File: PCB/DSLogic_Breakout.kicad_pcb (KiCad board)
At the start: 2 copper layers, 5 parts, among them J1 Interconnect

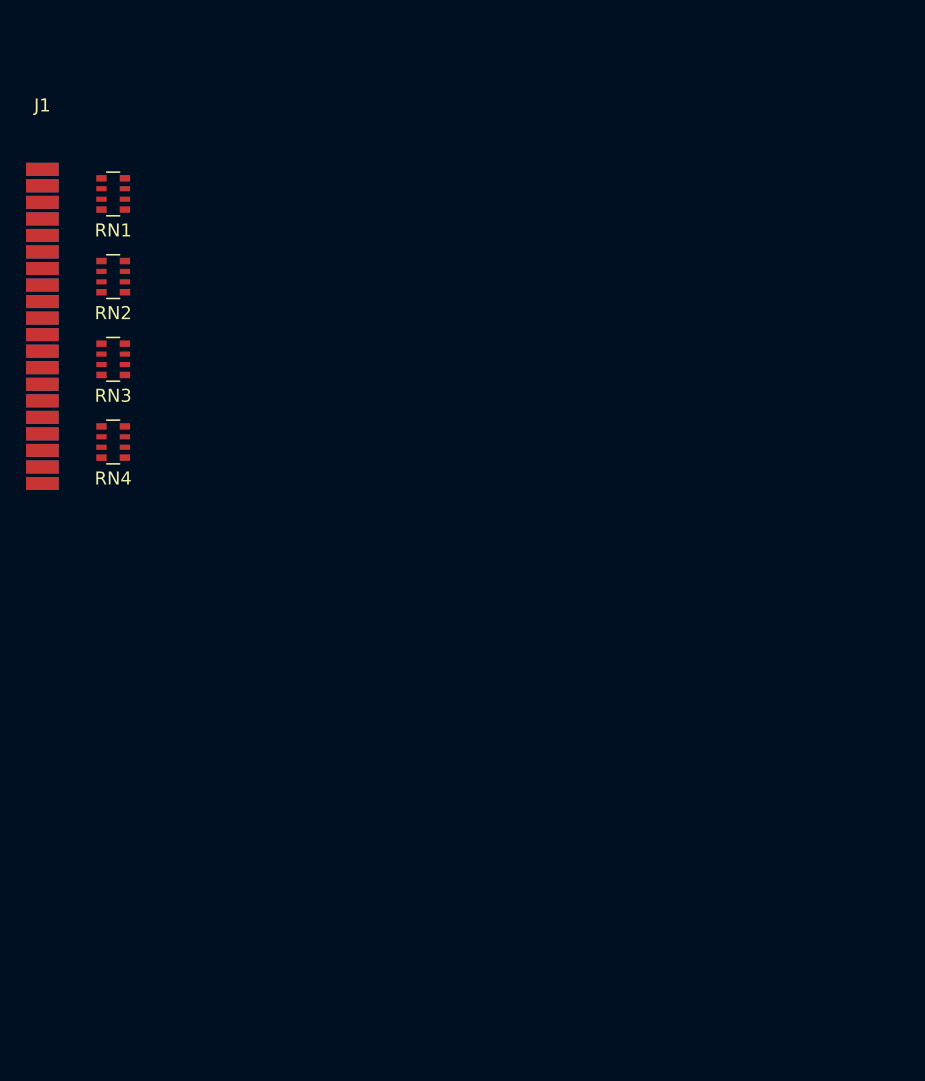
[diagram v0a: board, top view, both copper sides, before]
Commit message: Board max size measured
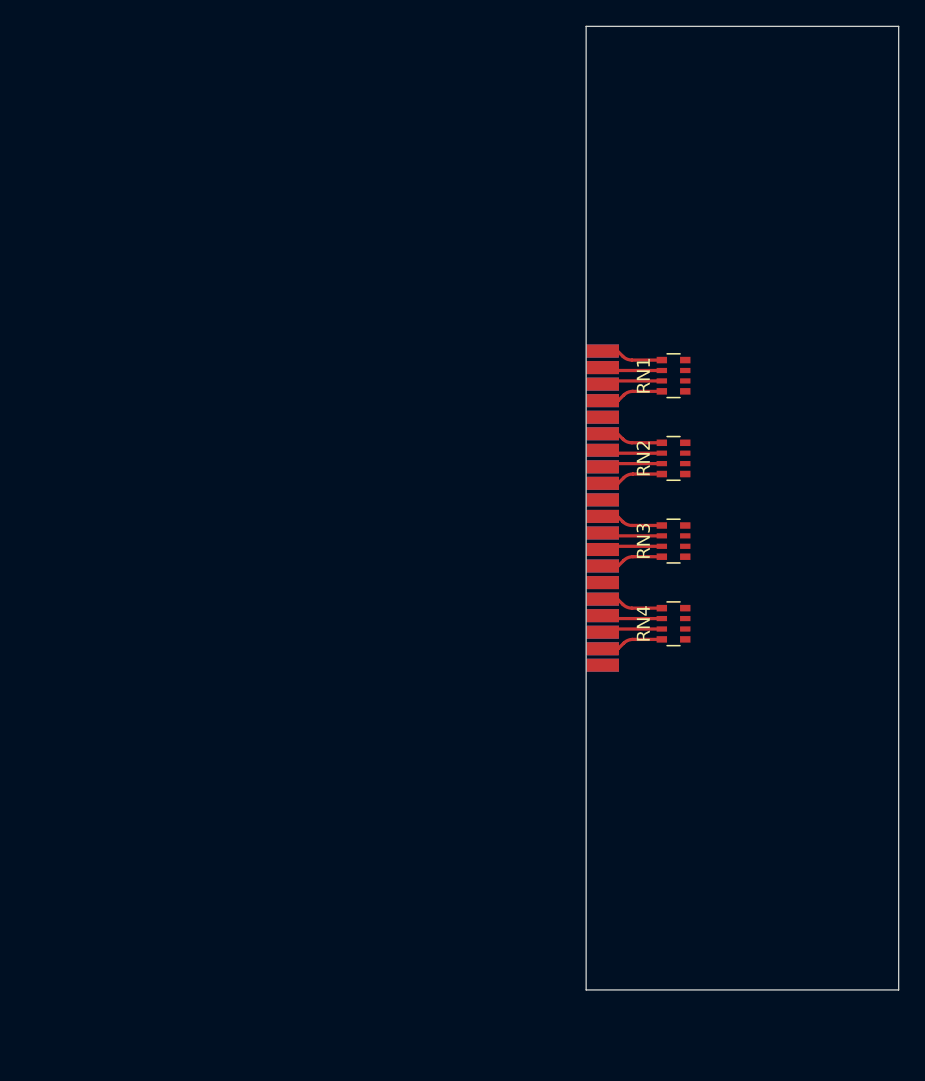
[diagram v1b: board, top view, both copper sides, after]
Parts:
- moved RN2 45.2 mm to (150.5, 59.9)
- moved RN3 45.2 mm to (150.5, 66.3)
- moved J1 45.2 mm to (145.0, 63.8)
- moved RN1 45.2 mm to (150.5, 53.6)
- moved RN4 45.2 mm to (150.5, 72.6)
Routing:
- net Net-(J1-Pin_7): track 0.00 -> 4.79 mm
- net Net-(J1-Pin_27): track 0.00 -> 4.79 mm
- net Net-(J1-Pin_17): track 0.00 -> 4.79 mm
- net Net-(J1-Pin_37): track 0.00 -> 4.79 mm
- net Net-(J1-Pin_11): track 0.00 -> 4.78 mm
- net Net-(J1-Pin_21): track 0.00 -> 4.78 mm
- net Net-(J1-Pin_1): track 0.00 -> 4.78 mm
- net Net-(J1-Pin_31): track 0.00 -> 4.78 mm
- net Net-(J1-Pin_5): track 0.00 -> 4.64 mm
- net Net-(J1-Pin_15): track 0.00 -> 4.64 mm
- net Net-(J1-Pin_35): track 0.00 -> 4.64 mm
- net Net-(J1-Pin_25): track 0.00 -> 4.64 mm
- net Net-(J1-Pin_33): track 0.00 -> 4.63 mm
- net Net-(J1-Pin_13): track 0.00 -> 4.63 mm
- net Net-(J1-Pin_3): track 0.00 -> 4.63 mm
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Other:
- board outline added: 24 x 74 mm
- board text added: "PCB Max Height: 74mm"

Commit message: Rev 1 Done
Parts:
- added ?: , , F.Cu at (141.1, 102.9)
- added ?: , , F.Cu at (123.3, 102.9)
- added ?: , , F.Cu at (125.9, 102.9)
- added ?: , , F.Cu at (133.5, 102.9)
- added ?: , , F.Cu at (141.1, 54.6)
- added ?: , , F.Cu at (133.5, 54.6)
- added ?: , , F.Cu at (151.3, 102.9)
- added ?: , , F.Cu at (146.2, 54.6)
- added ?: , , F.Cu at (156.3, 54.6)
- added ?: , , F.Cu at (138.6, 54.6)
- added ?: , , F.Cu at (136.0, 54.6)
- added ?: , , F.Cu at (151.3, 54.6)
- added ?: , , F.Cu at (123.3, 54.6)
- added ?: , , F.Cu at (146.2, 102.9)
- added ?: , , F.Cu at (148.7, 54.6)
- added ?: , , F.Cu at (153.8, 102.9)
- added ?: , , F.Cu at (130.9, 102.9)
- added ?: , , F.Cu at (130.9, 54.6)
- added ?: , , F.Cu at (120.8, 102.9)
- added ?: , , F.Cu at (128.4, 54.6)
- added ?: , , F.Cu at (156.3, 102.9)
- added ?: , , F.Cu at (128.4, 102.9)
- added ?: , , F.Cu at (148.7, 102.9)
- added ?: , , F.Cu at (143.6, 54.6)
- added ?: , , F.Cu at (153.8, 54.6)
- added ?: , , F.Cu at (138.6, 102.9)
- added ?: , , F.Cu at (143.6, 102.9)
- added ?: , , F.Cu at (136.0, 102.9)
- added ?: , , F.Cu at (125.9, 54.6)
- added D1: PWR, LED_SMD:LED_0603_1608Metric, F.Cu at (107.1, 56.1)
- added J2: Conn_Input, Connector_PinSocket_2.54mm:PinSocket_1x20_P2.54mm_Vertical, F.Cu at (117.6, 54.6)
- added R1: 2K2, Resistor_SMD:R_0603_1608Metric, F.Cu at (107.1, 54.6)
- added REF**: Protoboard_Hole, Footprints:Protoboard_Hole, F.Cu at (125.9, 72.4)
- added REF**: Protoboard_Hole, Footprints:Protoboard_Hole, F.Cu at (156.3, 59.7)
- added REF**: Protoboard_Hole, Footprints:Protoboard_Hole, F.Cu at (128.4, 67.3)
- added REF**: Protoboard_Hole, Footprints:Protoboard_Hole, F.Cu at (125.9, 97.8)
- added REF**: Protoboard_Hole, Footprints:Protoboard_Hole, F.Cu at (128.4, 74.9)
- added REF**: Protoboard_Hole, Footprints:Protoboard_Hole, F.Cu at (156.3, 67.3)
- added REF**: Protoboard_Hole, Footprints:Protoboard_Hole, F.Cu at (141.1, 85.1)
- added REF**: Protoboard_Hole, Footprints:Protoboard_Hole, F.Cu at (133.5, 72.4)
- added REF**: Protoboard_Hole, Footprints:Protoboard_Hole, F.Cu at (141.1, 57.1)
- added REF**: Protoboard_Hole, Footprints:Protoboard_Hole, F.Cu at (123.3, 62.2)
- added REF**: Protoboard_Hole, Footprints:Protoboard_Hole, F.Cu at (141.1, 59.7)
- added REF**: Protoboard_Hole, Footprints:Protoboard_Hole, F.Cu at (128.4, 95.2)
- added REF**: Protoboard_Hole, Footprints:Protoboard_Hole, F.Cu at (146.2, 85.1)
- added REF**: Protoboard_Hole, Footprints:Protoboard_Hole, F.Cu at (156.3, 82.5)
- added REF**: Protoboard_Hole, Footprints:Protoboard_Hole, F.Cu at (120.8, 82.5)
- added REF**: Protoboard_Hole, Footprints:Protoboard_Hole, F.Cu at (148.7, 90.2)
- added REF**: Protoboard_Hole, Footprints:Protoboard_Hole, F.Cu at (146.2, 77.5)
- added REF**: Protoboard_Hole, Footprints:Protoboard_Hole, F.Cu at (151.3, 87.6)
- added REF**: Protoboard_Hole, Footprints:Protoboard_Hole, F.Cu at (151.3, 59.7)
- added REF**: Protoboard_Hole, Footprints:Protoboard_Hole, F.Cu at (143.6, 90.2)
- added REF**: Protoboard_Hole, Footprints:Protoboard_Hole, F.Cu at (153.8, 95.2)
- added REF**: Protoboard_Hole, Footprints:Protoboard_Hole, F.Cu at (138.6, 85.1)
- added REF**: Protoboard_Hole, Footprints:Protoboard_Hole, F.Cu at (125.9, 95.2)
- added REF**: Protoboard_Hole, Footprints:Protoboard_Hole, F.Cu at (125.9, 80.0)
- added REF**: Protoboard_Hole, Footprints:Protoboard_Hole, F.Cu at (143.6, 69.8)
- added REF**: Protoboard_Hole, Footprints:Protoboard_Hole, F.Cu at (123.3, 64.8)
- added REF**: Protoboard_Hole, Footprints:Protoboard_Hole, F.Cu at (128.4, 92.7)
- added REF**: Protoboard_Hole, Footprints:Protoboard_Hole, F.Cu at (156.3, 100.3)
- added REF**: Protoboard_Hole, Footprints:Protoboard_Hole, F.Cu at (136.0, 87.6)
- added REF**: Protoboard_Hole, Footprints:Protoboard_Hole, F.Cu at (123.3, 87.6)
- added REF**: Protoboard_Hole, Footprints:Protoboard_Hole, F.Cu at (156.3, 57.1)
- added REF**: Protoboard_Hole, Footprints:Protoboard_Hole, F.Cu at (156.3, 72.4)
- added REF**: Protoboard_Hole, Footprints:Protoboard_Hole, F.Cu at (151.3, 57.1)
- added REF**: Protoboard_Hole, Footprints:Protoboard_Hole, F.Cu at (133.5, 77.5)
- added REF**: Protoboard_Hole, Footprints:Protoboard_Hole, F.Cu at (153.8, 77.5)
- added REF**: Protoboard_Hole, Footprints:Protoboard_Hole, F.Cu at (120.8, 85.1)
- added REF**: Protoboard_Hole, Footprints:Protoboard_Hole, F.Cu at (123.3, 69.8)
- added REF**: Protoboard_Hole, Footprints:Protoboard_Hole, F.Cu at (146.2, 62.2)
- added REF**: Protoboard_Hole, Footprints:Protoboard_Hole, F.Cu at (128.4, 100.3)
- added REF**: Protoboard_Hole, Footprints:Protoboard_Hole, F.Cu at (151.3, 80.0)
- added REF**: Protoboard_Hole, Footprints:Protoboard_Hole, F.Cu at (130.9, 97.8)
- added REF**: Protoboard_Hole, Footprints:Protoboard_Hole, F.Cu at (130.9, 59.7)
- added REF**: Protoboard_Hole, Footprints:Protoboard_Hole, F.Cu at (130.9, 72.4)
- added REF**: Protoboard_Hole, Footprints:Protoboard_Hole, F.Cu at (141.1, 87.6)
- added REF**: Protoboard_Hole, Footprints:Protoboard_Hole, F.Cu at (120.8, 87.6)
- added REF**: Protoboard_Hole, Footprints:Protoboard_Hole, F.Cu at (141.1, 69.8)
- added REF**: Protoboard_Hole, Footprints:Protoboard_Hole, F.Cu at (148.7, 97.8)
- added REF**: Protoboard_Hole, Footprints:Protoboard_Hole, F.Cu at (130.9, 62.2)
- added REF**: Protoboard_Hole, Footprints:Protoboard_Hole, F.Cu at (141.1, 62.2)
- added REF**: Protoboard_Hole, Footprints:Protoboard_Hole, F.Cu at (133.5, 59.7)
- added REF**: Protoboard_Hole, Footprints:Protoboard_Hole, F.Cu at (138.6, 69.8)
- added REF**: Protoboard_Hole, Footprints:Protoboard_Hole, F.Cu at (130.9, 92.7)
- added REF**: Protoboard_Hole, Footprints:Protoboard_Hole, F.Cu at (148.7, 77.5)
- added REF**: Protoboard_Hole, Footprints:Protoboard_Hole, F.Cu at (125.9, 69.8)
- added REF**: Protoboard_Hole, Footprints:Protoboard_Hole, F.Cu at (120.8, 67.3)
- added REF**: Protoboard_Hole, Footprints:Protoboard_Hole, F.Cu at (120.8, 72.4)
- added REF**: Protoboard_Hole, Footprints:Protoboard_Hole, F.Cu at (156.3, 92.7)
- added REF**: Protoboard_Hole, Footprints:Protoboard_Hole, F.Cu at (148.7, 82.5)
- added REF**: Protoboard_Hole, Footprints:Protoboard_Hole, F.Cu at (133.5, 100.3)
- added REF**: Protoboard_Hole, Footprints:Protoboard_Hole, F.Cu at (120.8, 62.2)
- added REF**: Protoboard_Hole, Footprints:Protoboard_Hole, F.Cu at (148.7, 57.1)
- added REF**: Protoboard_Hole, Footprints:Protoboard_Hole, F.Cu at (153.8, 82.5)
- added REF**: Protoboard_Hole, Footprints:Protoboard_Hole, F.Cu at (153.8, 87.6)
- added REF**: Protoboard_Hole, Footprints:Protoboard_Hole, F.Cu at (125.9, 62.2)
- added REF**: Protoboard_Hole, Footprints:Protoboard_Hole, F.Cu at (120.8, 95.2)
- added REF**: Protoboard_Hole, Footprints:Protoboard_Hole, F.Cu at (136.0, 64.8)
- added REF**: Protoboard_Hole, Footprints:Protoboard_Hole, F.Cu at (130.9, 100.3)
- added REF**: Protoboard_Hole, Footprints:Protoboard_Hole, F.Cu at (130.9, 69.8)
- added REF**: Protoboard_Hole, Footprints:Protoboard_Hole, F.Cu at (123.3, 59.7)
- added REF**: Protoboard_Hole, Footprints:Protoboard_Hole, F.Cu at (128.4, 87.6)
- added REF**: Protoboard_Hole, Footprints:Protoboard_Hole, F.Cu at (148.7, 85.1)
- added REF**: Protoboard_Hole, Footprints:Protoboard_Hole, F.Cu at (143.6, 87.6)
- added REF**: Protoboard_Hole, Footprints:Protoboard_Hole, F.Cu at (148.7, 92.7)
- added REF**: Protoboard_Hole, Footprints:Protoboard_Hole, F.Cu at (123.3, 57.1)
- added REF**: Protoboard_Hole, Footprints:Protoboard_Hole, F.Cu at (153.8, 72.4)
- added REF**: Protoboard_Hole, Footprints:Protoboard_Hole, F.Cu at (130.9, 80.0)
- added REF**: Protoboard_Hole, Footprints:Protoboard_Hole, F.Cu at (123.3, 77.5)
- added REF**: Protoboard_Hole, Footprints:Protoboard_Hole, F.Cu at (141.1, 77.5)
- added REF**: Protoboard_Hole, Footprints:Protoboard_Hole, F.Cu at (146.2, 82.5)
- added REF**: Protoboard_Hole, Footprints:Protoboard_Hole, F.Cu at (153.8, 80.0)
- added REF**: Protoboard_Hole, Footprints:Protoboard_Hole, F.Cu at (146.2, 87.6)
- added REF**: Protoboard_Hole, Footprints:Protoboard_Hole, F.Cu at (153.8, 69.8)
- added REF**: Protoboard_Hole, Footprints:Protoboard_Hole, F.Cu at (136.0, 57.1)
- added REF**: Protoboard_Hole, Footprints:Protoboard_Hole, F.Cu at (143.6, 72.4)
- added REF**: Protoboard_Hole, Footprints:Protoboard_Hole, F.Cu at (123.3, 72.4)
- added REF**: Protoboard_Hole, Footprints:Protoboard_Hole, F.Cu at (146.2, 74.9)
- added REF**: Protoboard_Hole, Footprints:Protoboard_Hole, F.Cu at (120.8, 74.9)
- added REF**: Protoboard_Hole, Footprints:Protoboard_Hole, F.Cu at (128.4, 97.8)
- added REF**: Protoboard_Hole, Footprints:Protoboard_Hole, F.Cu at (136.0, 92.7)
- added REF**: Protoboard_Hole, Footprints:Protoboard_Hole, F.Cu at (153.8, 57.1)
- added REF**: Protoboard_Hole, Footprints:Protoboard_Hole, F.Cu at (136.0, 95.2)
- added REF**: Protoboard_Hole, Footprints:Protoboard_Hole, F.Cu at (156.3, 90.2)
- added REF**: Protoboard_Hole, Footprints:Protoboard_Hole, F.Cu at (125.9, 67.3)
- added REF**: Protoboard_Hole, Footprints:Protoboard_Hole, F.Cu at (125.9, 82.5)
- added REF**: Protoboard_Hole, Footprints:Protoboard_Hole, F.Cu at (141.1, 82.5)
- added REF**: Protoboard_Hole, Footprints:Protoboard_Hole, F.Cu at (151.3, 72.4)
- added REF**: Protoboard_Hole, Footprints:Protoboard_Hole, F.Cu at (151.3, 67.3)
- added REF**: Protoboard_Hole, Footprints:Protoboard_Hole, F.Cu at (156.3, 74.9)
- added REF**: Protoboard_Hole, Footprints:Protoboard_Hole, F.Cu at (151.3, 85.1)
- added REF**: Protoboard_Hole, Footprints:Protoboard_Hole, F.Cu at (133.5, 57.1)
- added REF**: Protoboard_Hole, Footprints:Protoboard_Hole, F.Cu at (156.3, 80.0)
- added REF**: Protoboard_Hole, Footprints:Protoboard_Hole, F.Cu at (128.4, 80.0)
- added REF**: Protoboard_Hole, Footprints:Protoboard_Hole, F.Cu at (128.4, 57.1)
- added REF**: Protoboard_Hole, Footprints:Protoboard_Hole, F.Cu at (123.3, 90.2)
- added REF**: Protoboard_Hole, Footprints:Protoboard_Hole, F.Cu at (148.7, 87.6)
- added REF**: Protoboard_Hole, Footprints:Protoboard_Hole, F.Cu at (120.8, 64.8)
- added REF**: Protoboard_Hole, Footprints:Protoboard_Hole, F.Cu at (148.7, 100.3)
- added REF**: Protoboard_Hole, Footprints:Protoboard_Hole, F.Cu at (153.8, 97.8)
- added REF**: Protoboard_Hole, Footprints:Protoboard_Hole, F.Cu at (143.6, 100.3)
- added REF**: Protoboard_Hole, Footprints:Protoboard_Hole, F.Cu at (146.2, 57.1)
- added REF**: Protoboard_Hole, Footprints:Protoboard_Hole, F.Cu at (148.7, 67.3)
- added REF**: Protoboard_Hole, Footprints:Protoboard_Hole, F.Cu at (123.3, 92.7)
- added REF**: Protoboard_Hole, Footprints:Protoboard_Hole, F.Cu at (125.9, 85.1)
- added REF**: Protoboard_Hole, Footprints:Protoboard_Hole, F.Cu at (153.8, 64.8)
- added REF**: Protoboard_Hole, Footprints:Protoboard_Hole, F.Cu at (151.3, 69.8)
- added REF**: Protoboard_Hole, Footprints:Protoboard_Hole, F.Cu at (143.6, 97.8)
- added REF**: Protoboard_Hole, Footprints:Protoboard_Hole, F.Cu at (138.6, 72.4)
- added REF**: Protoboard_Hole, Footprints:Protoboard_Hole, F.Cu at (136.0, 97.8)
- added REF**: Protoboard_Hole, Footprints:Protoboard_Hole, F.Cu at (151.3, 74.9)
- added REF**: Protoboard_Hole, Footprints:Protoboard_Hole, F.Cu at (143.6, 82.5)
- added REF**: Protoboard_Hole, Footprints:Protoboard_Hole, F.Cu at (143.6, 80.0)
- added REF**: Protoboard_Hole, Footprints:Protoboard_Hole, F.Cu at (130.9, 74.9)
- added REF**: Protoboard_Hole, Footprints:Protoboard_Hole, F.Cu at (141.1, 95.2)
- added REF**: Protoboard_Hole, Footprints:Protoboard_Hole, F.Cu at (143.6, 59.7)
- added REF**: Protoboard_Hole, Footprints:Protoboard_Hole, F.Cu at (136.0, 82.5)
- added REF**: Protoboard_Hole, Footprints:Protoboard_Hole, F.Cu at (148.7, 74.9)
- added REF**: Protoboard_Hole, Footprints:Protoboard_Hole, F.Cu at (123.3, 74.9)
- added REF**: Protoboard_Hole, Footprints:Protoboard_Hole, F.Cu at (146.2, 90.2)
- added REF**: Protoboard_Hole, Footprints:Protoboard_Hole, F.Cu at (120.8, 97.8)
- added REF**: Protoboard_Hole, Footprints:Protoboard_Hole, F.Cu at (156.3, 85.1)
- added REF**: Protoboard_Hole, Footprints:Protoboard_Hole, F.Cu at (138.6, 90.2)
- added REF**: Protoboard_Hole, Footprints:Protoboard_Hole, F.Cu at (136.0, 74.9)
- added REF**: Protoboard_Hole, Footprints:Protoboard_Hole, F.Cu at (130.9, 82.5)
- added REF**: Protoboard_Hole, Footprints:Protoboard_Hole, F.Cu at (151.3, 97.8)
- added REF**: Protoboard_Hole, Footprints:Protoboard_Hole, F.Cu at (146.2, 100.3)
- added REF**: Protoboard_Hole, Footprints:Protoboard_Hole, F.Cu at (136.0, 72.4)
- added REF**: Protoboard_Hole, Footprints:Protoboard_Hole, F.Cu at (128.4, 82.5)
- added REF**: Protoboard_Hole, Footprints:Protoboard_Hole, F.Cu at (125.9, 100.3)
- added REF**: Protoboard_Hole, Footprints:Protoboard_Hole, F.Cu at (141.1, 74.9)
- added REF**: Protoboard_Hole, Footprints:Protoboard_Hole, F.Cu at (151.3, 82.5)
- added REF**: Protoboard_Hole, Footprints:Protoboard_Hole, F.Cu at (138.6, 80.0)
- added REF**: Protoboard_Hole, Footprints:Protoboard_Hole, F.Cu at (146.2, 72.4)
- added REF**: Protoboard_Hole, Footprints:Protoboard_Hole, F.Cu at (146.2, 59.7)
- added REF**: Protoboard_Hole, Footprints:Protoboard_Hole, F.Cu at (138.6, 97.8)
- added REF**: Protoboard_Hole, Footprints:Protoboard_Hole, F.Cu at (138.6, 74.9)
- added REF**: Protoboard_Hole, Footprints:Protoboard_Hole, F.Cu at (130.9, 87.6)
- added REF**: Protoboard_Hole, Footprints:Protoboard_Hole, F.Cu at (133.5, 92.7)
- added REF**: Protoboard_Hole, Footprints:Protoboard_Hole, F.Cu at (141.1, 90.2)
- added REF**: Protoboard_Hole, Footprints:Protoboard_Hole, F.Cu at (156.3, 62.2)
- added REF**: Protoboard_Hole, Footprints:Protoboard_Hole, F.Cu at (138.6, 77.5)
- added REF**: Protoboard_Hole, Footprints:Protoboard_Hole, F.Cu at (130.9, 64.8)
- added REF**: Protoboard_Hole, Footprints:Protoboard_Hole, F.Cu at (146.2, 95.2)
- added REF**: Protoboard_Hole, Footprints:Protoboard_Hole, F.Cu at (128.4, 90.2)
- added REF**: Protoboard_Hole, Footprints:Protoboard_Hole, F.Cu at (136.0, 62.2)
- added REF**: Protoboard_Hole, Footprints:Protoboard_Hole, F.Cu at (133.5, 95.2)
- added REF**: Protoboard_Hole, Footprints:Protoboard_Hole, F.Cu at (120.8, 80.0)
- added REF**: Protoboard_Hole, Footprints:Protoboard_Hole, F.Cu at (125.9, 64.8)
- added REF**: Protoboard_Hole, Footprints:Protoboard_Hole, F.Cu at (120.8, 90.2)
- added REF**: Protoboard_Hole, Footprints:Protoboard_Hole, F.Cu at (136.0, 69.8)
- added REF**: Protoboard_Hole, Footprints:Protoboard_Hole, F.Cu at (156.3, 87.6)
- added REF**: Protoboard_Hole, Footprints:Protoboard_Hole, F.Cu at (120.8, 100.3)
- added REF**: Protoboard_Hole, Footprints:Protoboard_Hole, F.Cu at (151.3, 95.2)
- added REF**: Protoboard_Hole, Footprints:Protoboard_Hole, F.Cu at (141.1, 97.8)
- added REF**: Protoboard_Hole, Footprints:Protoboard_Hole, F.Cu at (130.9, 90.2)
- added REF**: Protoboard_Hole, Footprints:Protoboard_Hole, F.Cu at (148.7, 80.0)
- added REF**: Protoboard_Hole, Footprints:Protoboard_Hole, F.Cu at (130.9, 77.5)
- added REF**: Protoboard_Hole, Footprints:Protoboard_Hole, F.Cu at (156.3, 95.2)
- added REF**: Protoboard_Hole, Footprints:Protoboard_Hole, F.Cu at (138.6, 95.2)
- added REF**: Protoboard_Hole, Footprints:Protoboard_Hole, F.Cu at (143.6, 57.1)
- added REF**: Protoboard_Hole, Footprints:Protoboard_Hole, F.Cu at (130.9, 95.2)
- added REF**: Protoboard_Hole, Footprints:Protoboard_Hole, F.Cu at (141.1, 67.3)
- added REF**: Protoboard_Hole, Footprints:Protoboard_Hole, F.Cu at (133.5, 74.9)
- added REF**: Protoboard_Hole, Footprints:Protoboard_Hole, F.Cu at (148.7, 59.7)
- added REF**: Protoboard_Hole, Footprints:Protoboard_Hole, F.Cu at (125.9, 59.7)
- added REF**: Protoboard_Hole, Footprints:Protoboard_Hole, F.Cu at (138.6, 92.7)
- added REF**: Protoboard_Hole, Footprints:Protoboard_Hole, F.Cu at (136.0, 90.2)
- added REF**: Protoboard_Hole, Footprints:Protoboard_Hole, F.Cu at (138.6, 82.5)
- added REF**: Protoboard_Hole, Footprints:Protoboard_Hole, F.Cu at (148.7, 64.8)
- added REF**: Protoboard_Hole, Footprints:Protoboard_Hole, F.Cu at (153.8, 62.2)
- added REF**: Protoboard_Hole, Footprints:Protoboard_Hole, F.Cu at (138.6, 57.1)
- added REF**: Protoboard_Hole, Footprints:Protoboard_Hole, F.Cu at (153.8, 67.3)
- added REF**: Protoboard_Hole, Footprints:Protoboard_Hole, F.Cu at (138.6, 100.3)
- added REF**: Protoboard_Hole, Footprints:Protoboard_Hole, F.Cu at (138.6, 62.2)
- added REF**: Protoboard_Hole, Footprints:Protoboard_Hole, F.Cu at (133.5, 80.0)
- added REF**: Protoboard_Hole, Footprints:Protoboard_Hole, F.Cu at (125.9, 74.9)
- added REF**: Protoboard_Hole, Footprints:Protoboard_Hole, F.Cu at (146.2, 92.7)
- added REF**: Protoboard_Hole, Footprints:Protoboard_Hole, F.Cu at (153.8, 59.7)
- added REF**: Protoboard_Hole, Footprints:Protoboard_Hole, F.Cu at (133.5, 67.3)
- added REF**: Protoboard_Hole, Footprints:Protoboard_Hole, F.Cu at (128.4, 85.1)
- added REF**: Protoboard_Hole, Footprints:Protoboard_Hole, F.Cu at (146.2, 67.3)
- added REF**: Protoboard_Hole, Footprints:Protoboard_Hole, F.Cu at (123.3, 97.8)
- added REF**: Protoboard_Hole, Footprints:Protoboard_Hole, F.Cu at (133.5, 62.2)
- added REF**: Protoboard_Hole, Footprints:Protoboard_Hole, F.Cu at (133.5, 69.8)
- added REF**: Protoboard_Hole, Footprints:Protoboard_Hole, F.Cu at (151.3, 100.3)
- added REF**: Protoboard_Hole, Footprints:Protoboard_Hole, F.Cu at (143.6, 95.2)
- added REF**: Protoboard_Hole, Footprints:Protoboard_Hole, F.Cu at (136.0, 85.1)
- added REF**: Protoboard_Hole, Footprints:Protoboard_Hole, F.Cu at (141.1, 92.7)
- added REF**: Protoboard_Hole, Footprints:Protoboard_Hole, F.Cu at (138.6, 59.7)
- added REF**: Protoboard_Hole, Footprints:Protoboard_Hole, F.Cu at (153.8, 74.9)
- added REF**: Protoboard_Hole, Footprints:Protoboard_Hole, F.Cu at (141.1, 72.4)
- added REF**: Protoboard_Hole, Footprints:Protoboard_Hole, F.Cu at (151.3, 62.2)
- added REF**: Protoboard_Hole, Footprints:Protoboard_Hole, F.Cu at (123.3, 85.1)
- added REF**: Protoboard_Hole, Footprints:Protoboard_Hole, F.Cu at (156.3, 77.5)
- added REF**: Protoboard_Hole, Footprints:Protoboard_Hole, F.Cu at (143.6, 77.5)
- added REF**: Protoboard_Hole, Footprints:Protoboard_Hole, F.Cu at (123.3, 95.2)
- added REF**: Protoboard_Hole, Footprints:Protoboard_Hole, F.Cu at (133.5, 90.2)
- added REF**: Protoboard_Hole, Footprints:Protoboard_Hole, F.Cu at (146.2, 69.8)
- added REF**: Protoboard_Hole, Footprints:Protoboard_Hole, F.Cu at (128.4, 72.4)
- added REF**: Protoboard_Hole, Footprints:Protoboard_Hole, F.Cu at (125.9, 77.5)
- added REF**: Protoboard_Hole, Footprints:Protoboard_Hole, F.Cu at (133.5, 85.1)
- added REF**: Protoboard_Hole, Footprints:Protoboard_Hole, F.Cu at (151.3, 90.2)
- added REF**: Protoboard_Hole, Footprints:Protoboard_Hole, F.Cu at (148.7, 95.2)
- added REF**: Protoboard_Hole, Footprints:Protoboard_Hole, F.Cu at (143.6, 67.3)
- added REF**: Protoboard_Hole, Footprints:Protoboard_Hole, F.Cu at (143.6, 62.2)
- added REF**: Protoboard_Hole, Footprints:Protoboard_Hole, F.Cu at (123.3, 80.0)
- added REF**: Protoboard_Hole, Footprints:Protoboard_Hole, F.Cu at (138.6, 64.8)
- added REF**: Protoboard_Hole, Footprints:Protoboard_Hole, F.Cu at (120.8, 54.6)
- added REF**: Protoboard_Hole, Footprints:Protoboard_Hole, F.Cu at (125.9, 92.7)
- added REF**: Protoboard_Hole, Footprints:Protoboard_Hole, F.Cu at (133.5, 64.8)
- added REF**: Protoboard_Hole, Footprints:Protoboard_Hole, F.Cu at (120.8, 59.7)
- added REF**: Protoboard_Hole, Footprints:Protoboard_Hole, F.Cu at (125.9, 87.6)
- added REF**: Protoboard_Hole, Footprints:Protoboard_Hole, F.Cu at (123.3, 100.3)
- added REF**: Protoboard_Hole, Footprints:Protoboard_Hole, F.Cu at (130.9, 85.1)
- added REF**: Protoboard_Hole, Footprints:Protoboard_Hole, F.Cu at (136.0, 77.5)
- added REF**: Protoboard_Hole, Footprints:Protoboard_Hole, F.Cu at (146.2, 64.8)
- added REF**: Protoboard_Hole, Footprints:Protoboard_Hole, F.Cu at (125.9, 57.1)
- added REF**: Protoboard_Hole, Footprints:Protoboard_Hole, F.Cu at (138.6, 87.6)
- added REF**: Protoboard_Hole, Footprints:Protoboard_Hole, F.Cu at (125.9, 90.2)
- added REF**: Protoboard_Hole, Footprints:Protoboard_Hole, F.Cu at (128.4, 62.2)
- added REF**: Protoboard_Hole, Footprints:Protoboard_Hole, F.Cu at (120.8, 92.7)
- added REF**: Protoboard_Hole, Footprints:Protoboard_Hole, F.Cu at (130.9, 67.3)
- added REF**: Protoboard_Hole, Footprints:Protoboard_Hole, F.Cu at (133.5, 97.8)
- added REF**: Protoboard_Hole, Footprints:Protoboard_Hole, F.Cu at (156.3, 64.8)
- added REF**: Protoboard_Hole, Footprints:Protoboard_Hole, F.Cu at (128.4, 77.5)
- added REF**: Protoboard_Hole, Footprints:Protoboard_Hole, F.Cu at (136.0, 100.3)
- added REF**: Protoboard_Hole, Footprints:Protoboard_Hole, F.Cu at (138.6, 67.3)
- added REF**: Protoboard_Hole, Footprints:Protoboard_Hole, F.Cu at (120.8, 57.1)
- added REF**: Protoboard_Hole, Footprints:Protoboard_Hole, F.Cu at (123.3, 67.3)
- added REF**: Protoboard_Hole, Footprints:Protoboard_Hole, F.Cu at (148.7, 69.8)
- added REF**: Protoboard_Hole, Footprints:Protoboard_Hole, F.Cu at (153.8, 100.3)
- added REF**: Protoboard_Hole, Footprints:Protoboard_Hole, F.Cu at (120.8, 77.5)
- added REF**: Protoboard_Hole, Footprints:Protoboard_Hole, F.Cu at (151.3, 64.8)
- added REF**: Protoboard_Hole, Footprints:Protoboard_Hole, F.Cu at (151.3, 92.7)
- added REF**: Protoboard_Hole, Footprints:Protoboard_Hole, F.Cu at (153.8, 90.2)
- added REF**: Protoboard_Hole, Footprints:Protoboard_Hole, F.Cu at (156.3, 97.8)
- added REF**: Protoboard_Hole, Footprints:Protoboard_Hole, F.Cu at (143.6, 64.8)
- added REF**: Protoboard_Hole, Footprints:Protoboard_Hole, F.Cu at (153.8, 92.7)
- added REF**: Protoboard_Hole, Footprints:Protoboard_Hole, F.Cu at (136.0, 59.7)
- added REF**: Protoboard_Hole, Footprints:Protoboard_Hole, F.Cu at (120.8, 69.8)
- added REF**: Protoboard_Hole, Footprints:Protoboard_Hole, F.Cu at (133.5, 82.5)
- added REF**: Protoboard_Hole, Footprints:Protoboard_Hole, F.Cu at (148.7, 72.4)
- added REF**: Protoboard_Hole, Footprints:Protoboard_Hole, F.Cu at (133.5, 87.6)
- added REF**: Protoboard_Hole, Footprints:Protoboard_Hole, F.Cu at (141.1, 80.0)
- added REF**: Protoboard_Hole, Footprints:Protoboard_Hole, F.Cu at (136.0, 67.3)
- added REF**: Protoboard_Hole, Footprints:Protoboard_Hole, F.Cu at (148.7, 62.2)
- added REF**: Protoboard_Hole, Footprints:Protoboard_Hole, F.Cu at (123.3, 82.5)
- added REF**: Protoboard_Hole, Footprints:Protoboard_Hole, F.Cu at (143.6, 74.9)
- added REF**: Protoboard_Hole, Footprints:Protoboard_Hole, F.Cu at (156.3, 69.8)
- added REF**: Protoboard_Hole, Footprints:Protoboard_Hole, F.Cu at (146.2, 80.0)
- added REF**: Protoboard_Hole, Footprints:Protoboard_Hole, F.Cu at (153.8, 85.1)
- added REF**: Protoboard_Hole, Footprints:Protoboard_Hole, F.Cu at (128.4, 64.8)
- added REF**: Protoboard_Hole, Footprints:Protoboard_Hole, F.Cu at (136.0, 80.0)
- added REF**: Protoboard_Hole, Footprints:Protoboard_Hole, F.Cu at (141.1, 100.3)
- added REF**: Protoboard_Hole, Footprints:Protoboard_Hole, F.Cu at (128.4, 69.8)
- added REF**: Protoboard_Hole, Footprints:Protoboard_Hole, F.Cu at (143.6, 85.1)
- added REF**: Protoboard_Hole, Footprints:Protoboard_Hole, F.Cu at (141.1, 64.8)
- added REF**: Protoboard_Hole, Footprints:Protoboard_Hole, F.Cu at (130.9, 57.1)
- added REF**: Protoboard_Hole, Footprints:Protoboard_Hole, F.Cu at (146.2, 97.8)
- added REF**: Protoboard_Hole, Footprints:Protoboard_Hole, F.Cu at (143.6, 92.7)
- added REF**: Protoboard_Hole, Footprints:Protoboard_Hole, F.Cu at (128.4, 59.7)
- added REF**: Protoboard_Hole, Footprints:Protoboard_Hole, F.Cu at (151.3, 77.5)
- moved RN1 43.8 mm to (109.6, 69.2)
- moved RN2 43.8 mm to (109.6, 75.6)
- moved RN3 43.8 mm to (109.6, 81.9)
- moved RN4 43.8 mm to (109.6, 88.3)
- moved J1 43.8 mm to (104.1, 79.4)
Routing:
- net +3.3V: track 0.00 -> 143.1 mm, vias 0 -> 1
- net GND: track 0.00 -> 112.4 mm, vias 0 -> 12
- net /INPUT_00: track 0.00 -> 11.3 mm
- net /INPUT_15: track 0.00 -> 11.3 mm
- net /INPUT_14: track 0.00 -> 10.1 mm
- net /INPUT_01: track 0.00 -> 10.1 mm
- net /INPUT_02: track 0.00 -> 9.06 mm
- net /INPUT_13: track 0.00 -> 9.06 mm
- net /INPUT_04: track 0.00 -> 8.92 mm
- net /INPUT_11: track 0.00 -> 8.92 mm
- net /INPUT_12: track 0.00 -> 8.26 mm
- net /INPUT_03: track 0.00 -> 8.26 mm
- net /INPUT_10: track 0.00 -> 8.20 mm
- net /INPUT_05: track 0.00 -> 8.20 mm
- net /INPUT_09: track 0.00 -> 7.48 mm
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- added copper zone on B.Cu, net GND
- added copper zone on F.Cu, net GND
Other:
- board size 24 x 74 mm -> 56 x 54 mm
- board text added: "3.3V"
- board text added: "GND"
- board text added: "IN-00"
- board text added: "IN-01"
- board text added: "IN-02"
- board text added: "IN-03"
- board text added: "IN-04"
- board text added: "IN-05"
- board text added: "IN-06"
- board text added: "IN-07"
- board text added: "IN-08"
- board text added: "IN-09"
- board text added: "IN-10"
- board text added: "IN-11"
- board text added: "IN-12"
- board text added: "IN-13"
- board text added: "IN-14"
- board text added: "IN-15"
- board text added: "PWR"
- board text removed: "PCB Max Height: 74mm"
